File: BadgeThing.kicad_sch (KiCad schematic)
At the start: 67 parts, among them J10 Conn_01x01, J11 Conn_01x01, J12 Conn_01x01, J2 Ext 5V, J3 External 3V3, J4 SWD Header, J5 USB_C_Receptacle_USB2.0, J6 Connector_Generic_Conn_01x02, J7 Conn_01x06, J8 Conn_01x01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

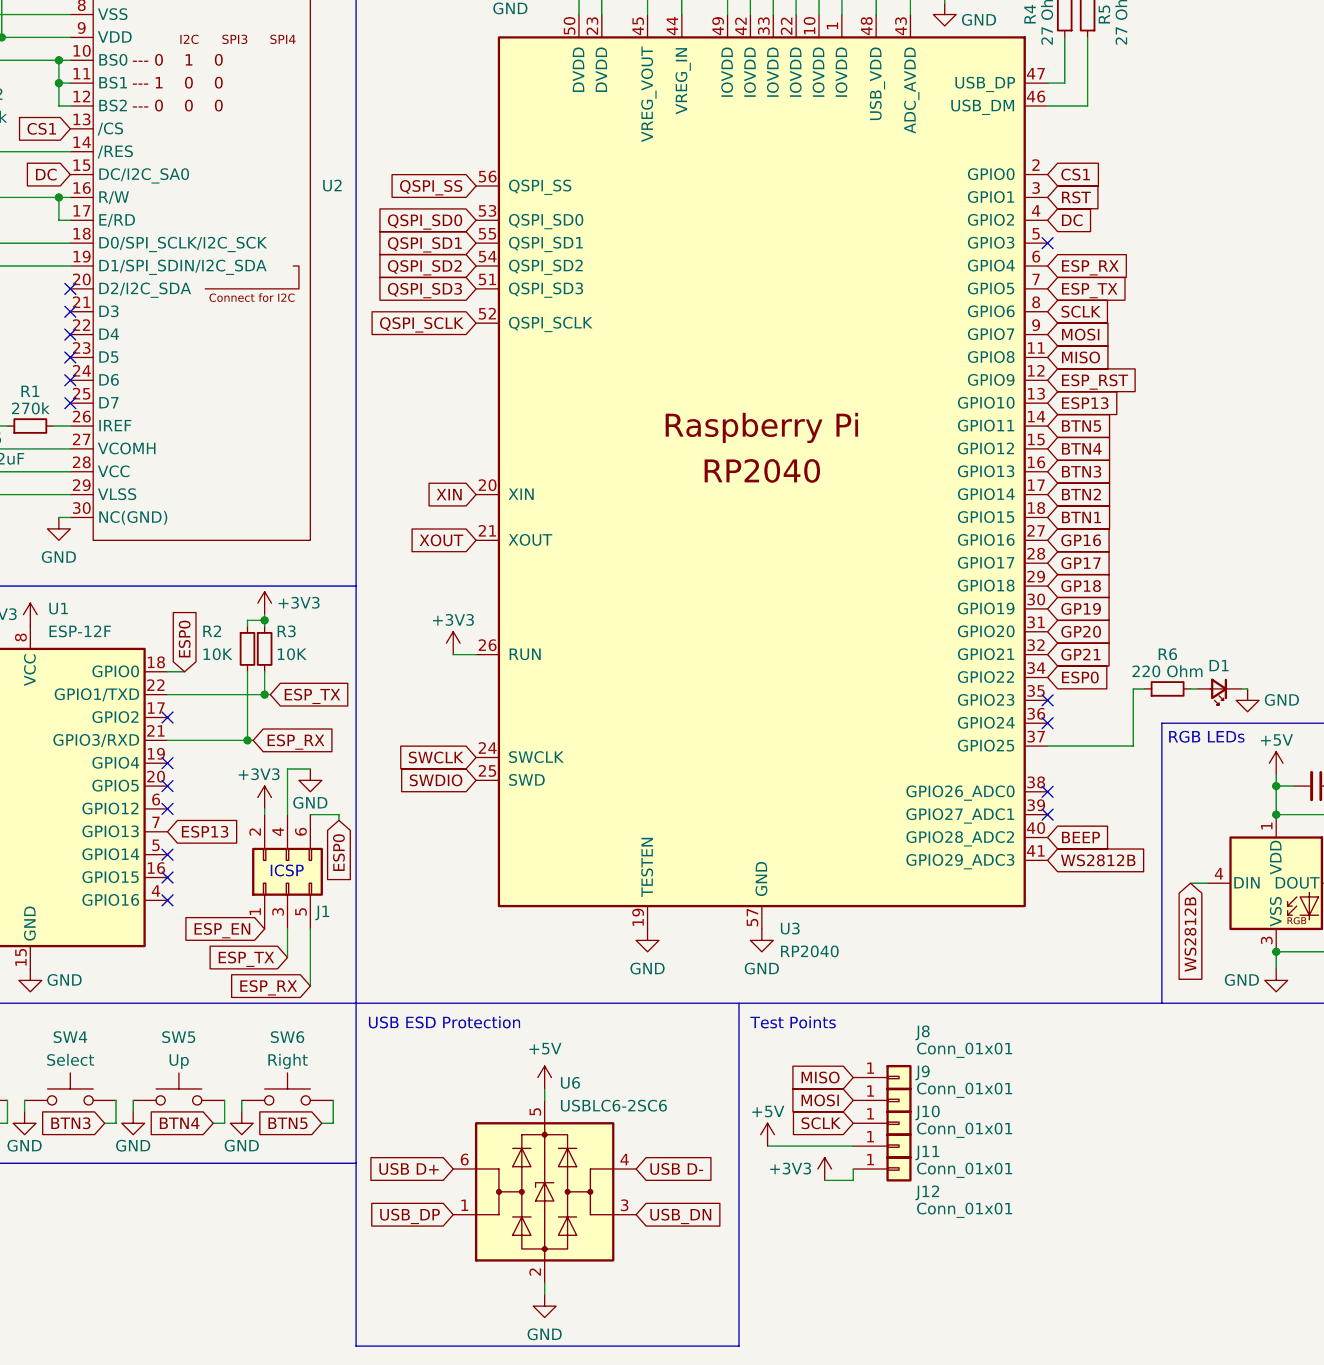
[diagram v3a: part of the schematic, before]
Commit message: Fix SPI wiring, add ESP RTS pin, add prod files
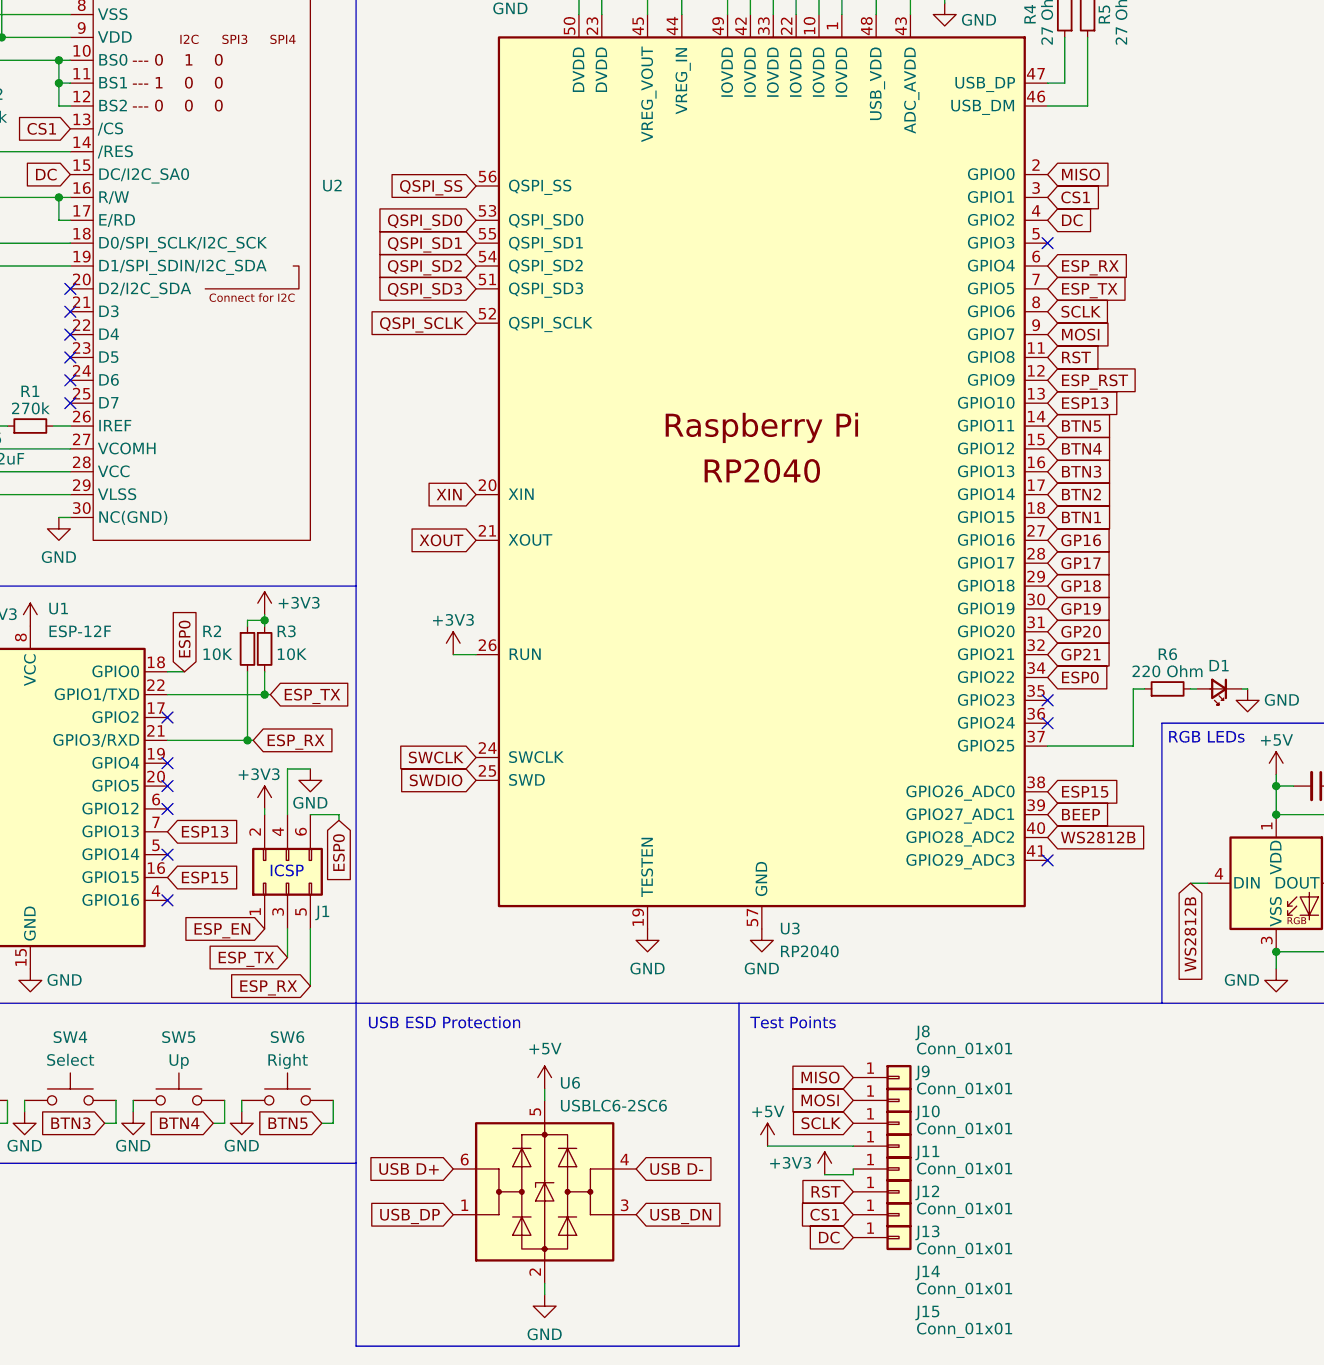
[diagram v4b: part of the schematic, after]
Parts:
- added J13, J14, J15: Conn_01x01, Connector_PinHeader_2.00mm:PinHeader_1x01_P2.00mm_Vertical, symbol Connector_Generic:Conn_01x01
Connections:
- net BEEP: now also U3.39 (GPIO27_ADC1); no longer U3.40 (GPIO28_ADC2)
- net CS1: now also U3.3 (GPIO1), J14.1 (Pin_1); no longer U3.2 (GPIO0)
- net DC: now also J15.1 (Pin_1)
- net MISO: now also U3.2 (GPIO0); no longer U3.11 (GPIO8)
- net RST: now also U3.11 (GPIO8), J13.1 (Pin_1); no longer U3.3 (GPIO1)
- net WS2812B: now also U3.40 (GPIO28_ADC2); no longer U3.41 (GPIO29_ADC3)
- net ESP15: now reaches U3.38 (GPIO26_ADC0)
- net ESP15: now also U1.16 (GPIO15)
- no-connect marks 29 -> 27
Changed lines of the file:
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@@
   )
   (no_connect (at 269.875 100.33))
+  (no_connect (at 153.67 66.04))
   (no_connect (at 55.88 139.065))
-  (no_connect (at 153.67 127))
   (no_connect (at 45.085 83.82))
   (no_connect (at 55.88 133.985))
@@
   (no_connect (at 55.88 118.745))
   (no_connect (at 25.4 133.985))
-  (no_connect (at 55.88 136.525))
   (no_connect (at 25.4 136.525))
   (no_connect (at 269.875 102.87))
@@
   (no_connect (at 55.88 123.825))
   (no_connect (at 55.88 128.905))
+  (no_connect (at 153.67 134.62))
   (no_connect (at 45.085 76.2))
-  (no_connect (at 153.67 66.04))
-  (no_connect (at 153.67 129.54))
   (no_connect (at 153.67 119.38))
   (no_connect (at 153.67 116.84))
@@
     (stroke (width 0) (type default))
   )
-  (wire (pts (xy 132.08 170.18) (xy 128.905 170.18))
+  (wire (pts (xy 132.08 169.545) (xy 128.905 169.545))
     (stroke (width 0) (type default))
   )
@@
     (stroke (width 0) (type default))
   )
-  (wire (pts (xy 132.08 168.91) (xy 132.08 170.18))
+  (wire (pts (xy 132.08 168.91) (xy 132.08 169.545))
     (stroke (width 0) (type default))
   )
@@
     )
   )
-  (global_label "WS2812B" (shape input) (at 153.67 134.62 0) (fields_autoplaced)
-    (effects (font (size 1.27 1.27)) (justify left))
-    (property "Intersheetrefs" "${INTERSHEET_REFS}" (at 165.3447 134.62 0)
-      (effects (font (size 1.27 1.27)) (justify left) hide)
-    )
-  )
   (global_label "QSPI_SD0" (shape input) (at 90.17 63.5 180) (fields_autoplaced)
     (effects (font (size 1.27 1.27)) (justify right))
@@
     )
   )
+  (global_label "DC" (shape input) (at 132.08 176.53 180) (fields_autoplaced)
+    (effects (font (size 1.27 1.27)) (justify right))
+    (property "Intersheetrefs" "${INTERSHEET_REFS}" (at 126.6342 176.53 0)
+      (effects (font (size 1.27 1.27)) (justify right) hide)
+    )
+  )
   (global_label "QSPI_SCLK" (shape input) (at 241.935 43.815 270) (fields_autoplaced)
     (effects (font (size 1.27 1.27)) (justify right))
@@
     )
   )
+  (global_label "ESP15" (shape input) (at 55.88 136.525 0) (fields_autoplaced)
+    (effects (font (size 1.27 1.27)) (justify left))
+    (property "Intersheetrefs" "${INTERSHEET_REFS}" (at 64.8333 136.525 0)
+      (effects (font (size 1.27 1.27)) (justify left) hide)
+    )
+  )
   (global_label "QSPI_SD3" (shape input) (at 271.145 46.355 0) (fields_autoplaced)
     (effects (font (size 1.27 1.27)) (justify left))
@@
     )
   )
+  (global_label "CS1" (shape input) (at 132.08 173.99 180) (fields_autoplaced)
+    (effects (font (size 1.27 1.27)) (justify right))
+    (property "Intersheetrefs" "${INTERSHEET_REFS}" (at 125.4852 173.99 0)
+      (effects (font (size 1.27 1.27)) (justify right) hide)
+    )
+  )
   (global_label "QSPI_SD3" (shape input) (at 90.17 71.12 180) (fields_autoplaced)
     (effects (font (size 1.27 1.27)) (justify right))
@@
     )
   )
-  (global_label "RST" (shape input) (at 153.67 60.96 0) (fields_autoplaced)
+  (global_label "RST" (shape input) (at 153.67 78.74 0) (fields_autoplaced)
     (effects (font (size 1.27 1.27)) (justify left))
     (property "Intersheetrefs" "${INTERSHEET_REFS}" (at 160.0229 60.96 0)
@@
     )
   )
+  (global_label "ESP15" (shape input) (at 153.67 127 0) (fields_autoplaced)
+    (effects (font (size 1.27 1.27)) (justify left))
+    (property "Intersheetrefs" "${INTERSHEET_REFS}" (at 162.6233 127 0)
+      (effects (font (size 1.27 1.27)) (justify left) hide)
+    )
+  )
   (global_label "SWCLK" (shape input) (at 90.17 123.19 180) (fields_autoplaced)
     (effects (font (size 1.27 1.27)) (justify right))
@@
     )
   )
-  (global_label "CS1" (shape input) (at 153.67 58.42 0) (fields_autoplaced)
+  (global_label "CS1" (shape input) (at 153.67 60.96 0) (fields_autoplaced)
     (effects (font (size 1.27 1.27)) (justify left))
     (property "Intersheetrefs" "${INTERSHEET_REFS}" (at 160.2648 58.42 0)
@@
     )
   )
-  (global_label "MISO" (shape input) (at 153.67 78.74 0) (fields_autoplaced)
+  (global_label "MISO" (shape input) (at 153.67 58.42 0) (fields_autoplaced)
     (effects (font (size 1.27 1.27)) (justify left))
     (property "Intersheetrefs" "${INTERSHEET_REFS}" (at 161.172 78.74 0)
@@
     )
   )
+  (global_label "RST" (shape input) (at 132.08 171.45 180) (fields_autoplaced)
+    (effects (font (size 1.27 1.27)) (justify right))
+    (property "Intersheetrefs" "${INTERSHEET_REFS}" (at 125.7271 171.45 0)
+      (effects (font (size 1.27 1.27)) (justify right) hide)
+    )
+  )
   (global_label "QSPI_SS" (shape input) (at 90.17 59.69 180) (fields_autoplaced)
     (effects (font (size 1.27 1.27)) (justify right))
@@
     )
   )
+  (global_label "BEEP" (shape input) (at 153.67 129.54 0) (fields_autoplaced)
+    (effects (font (size 1.27 1.27)) (justify left))
+    (property "Intersheetrefs" "${INTERSHEET_REFS}" (at 161.4138 129.54 0)
+      (effects (font (size 1.27 1.27)) (justify left) hide)
+    )
+  )
   (global_label "XIN" (shape input) (at 90.17 93.98 180) (fields_autoplaced)
     (effects (font (size 1.27 1.27)) (justify right))
@@
     )
   )
+  (global_label "WS2812B" (shape input) (at 153.67 132.08 0) (fields_autoplaced)
+    (effects (font (size 1.27 1.27)) (justify left))
+    (property "Intersheetrefs" "${INTERSHEET_REFS}" (at 165.3447 132.08 0)
+      (effects (font (size 1.27 1.27)) (justify left) hide)
+    )
+  )
   (global_label "BTN3" (shape input) (at 48.895 163.83 180) (fields_autoplaced)
     (effects (font (size 1.27 1.27)) (justify right))
@@
     (effects (font (size 1.27 1.27)) (justify left))
     (property "Intersheetrefs" "${INTERSHEET_REFS}" (at 281.1781 92.6306 0)
-      (effects (font (size 1.27 1.27)) (justify left) hide)
-    )
-  )
-  (global_label "BEEP" (shape input) (at 153.67 132.08 0) (fields_autoplaced)
-    (effects (font (size 1.27 1.27)) (justify left))
-    (property "Intersheetrefs" "${INTERSHEET_REFS}" (at 161.4138 132.08 0)
       (effects (font (size 1.27 1.27)) (justify left) hide)
     )
@@
     )
   )
-  (symbol (lib_id "power:+3V3") (at 128.905 170.18 0) (unit 1)
-    (in_bom yes) (on_board yes) (dnp no)
-    (property "Reference" "#PWR047" (at 128.905 173.99 0)
-      (effects (font (size 1.27 1.27)) hide)
-    )
-    (property "Value" "+3V3" (at 125.095 168.91 0)
-      (effects (font (size 1.27 1.27)))
-    )
-    (property "Footprint" "" (at 128.905 170.18 0)
-      (effects (font (size 1.27 1.27)) hide)
-    )
-    (property "Datasheet" "" (at 128.905 170.18 0)
+  (symbol (lib_id "power:+3V3") (at 128.905 169.545 0) (unit 1)
+    (in_bom yes) (on_board yes) (dnp no)
+    (property "Reference" "#PWR047" (at 128.905 173.355 0)
+      (effects (font (size 1.27 1.27)) hide)
+    )
+    (property "Value" "+3V3" (at 125.095 168.275 0)
+      (effects (font (size 1.27 1.27)))
+    )
+    (property "Footprint" "" (at 128.905 169.545 0)
+      (effects (font (size 1.27 1.27)) hide)
+    )
+    (property "Datasheet" "" (at 128.905 169.545 0)
       (effects (font (size 1.27 1.27)) hide)
     )
@@
     )
   )
+  (symbol (lib_id "Connector_Generic:Conn_01x01") (at 137.16 176.53 0) (unit 1)
+    (in_bom yes) (on_board yes) (dnp no)
+    (property "Reference" "J15" (at 139.065 184.785 0)
+      (effects (font (size 1.27 1.27)) (justify left))
+    )
+    (property "Value" "Conn_01x01" (at 139.065 186.69 0)
+      (effects (font (size 1.27 1.27)) (justify left))
+    )
+    (property "Footprint" "Connector_PinHeader_2.00mm:PinHeader_1x01_P2.00mm_Vertical" (at 137.16 176.53 0)
+      (effects (font (size 1.27 1.27)) hide)
+    )
+    (property "Datasheet" "~" (at 137.16 176.53 0)
+      (effects (font (size 1.27 1.27)) hide)
+    )
+    (pin "1")
+    (instances
+      (project "BadgeThing"
+        (path "/35d5f6bf-e39e-48ab-813a-17587fce37db"
+          (reference "J15") (unit 1)
+        )
+      )
+    )
+  )
   (symbol (lib_id "Device:C_Small") (at 83.185 26.035 0) (unit 1)
     (in_bom yes) (on_board yes) (dnp no)
@@
         (path "/35d5f6bf-e39e-48ab-813a-17587fce37db"
           (reference "SW6") (unit 1)
+        )
+      )
+    )
+  )
+  (symbol (lib_id "Connector_Generic:Conn_01x01") (at 137.16 173.99 0) (unit 1)
+    (in_bom yes) (on_board yes) (dnp no)
+    (property "Reference" "J14" (at 139.065 180.34 0)
+      (effects (font (size 1.27 1.27)) (justify left))
+    )
+    (property "Value" "Conn_01x01" (at 139.065 182.245 0)
+      (effects (font (size 1.27 1.27)) (justify left))
+    )
+    (property "Footprint" "Connector_PinHeader_2.00mm:PinHeader_1x01_P2.00mm_Vertical" (at 137.16 173.99 0)
+      (effects (font (size 1.27 1.27)) hide)
+    )
+    (property "Datasheet" "~" (at 137.16 173.99 0)
+      (effects (font (size 1.27 1.27)) hide)
+    )
+    (pin "1")
+    (instances
+      (project "BadgeThing"
+        (path "/35d5f6bf-e39e-48ab-813a-17587fce37db"
+          (reference "J14") (unit 1)
         )
       )
@@
         )
       )
+    )
+  )
+  (symbol (lib_id "Connector_Generic:Conn_01x01") (at 137.16 171.45 0) (unit 1)
+    (in_bom yes) (on_board yes) (dnp no)
+    (property "Reference" "J13" (at 139.065 175.895 0)
+      (effects (font (size 1.27 1.27)) (justify left))
+    )
+    (property "Value" "Conn_01x01" (at 139.065 177.8 0)
+      (effects (font (size 1.27 1.27)) (justify left))
+    )
+    (property "Footprint" "Connector_PinHeader_2.00mm:PinHeader_1x01_P2.00mm_Vertical" (at 137.16 171.45 0)
+      (effects (font (size 1.27 1.27)) hide)
+    )
+    (property "Datasheet" "~" (at 137.16 171.45 0)
+      (effects (font (size 1.27 1.27)) hide)
+    )
+    (pin "1")
+    (instances
+      (project "BadgeThing"
+        (path "/35d5f6bf-e39e-48ab-813a-17587fce37db"
+          (reference "J13") (unit 1)
+        )
+      )
